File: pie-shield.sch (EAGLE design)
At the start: 15 parts, among them IC6 78L05, IC8 MAX487, X6 RJ45-8L-B

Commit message: before wiring to raspberry
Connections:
- net N$35 renamed SELECT
- net +5V: now also U$2.5V@2, U$2.5V@4, U$2.5V@P5_1
- net GND: now also U$2.GND@14, U$2.GND@20, U$2.GND@6, U$2.GND@P5_7, U$2.GND@P5_8
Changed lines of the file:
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@@
 <pinref part="R22" gate="G$1" pin="1"/>
 <pinref part="R19" gate="G$1" pin="1"/>
+<label x="-33.02" y="78.74" size="1.778" layer="95"/>
+</segment>
+<segment>
+<pinref part="U$2" gate="G$1" pin="5V@2"/>
+<pinref part="U$2" gate="G$1" pin="5V@4"/>
+<wire x1="-73.66" y1="73.66" x2="-86.36" y2="73.66" width="0.1524" layer="91"/>
+<wire x1="-86.36" y1="73.66" x2="-86.36" y2="71.12" width="0.1524" layer="91"/>
+<wire x1="-86.36" y1="71.12" x2="-73.66" y2="71.12" width="0.1524" layer="91"/>
+<label x="-73.66" y="71.12" size="1.778" layer="95"/>
+<label x="-73.66" y="73.66" size="1.778" layer="95"/>
+</segment>
+<segment>
+<pinref part="U$2" gate="G$1" pin="5V@P5_1"/>
+<wire x1="-142.24" y1="38.1" x2="-149.86" y2="38.1" width="0.1524" layer="91"/>
+<label x="-154.94" y="38.1" size="1.778" layer="95"/>
 </segment>
 </net>
-<net name="N$35" class="0">
+<net name="SELECT" class="0">
 <segment>
 <wire x1="-17.78" y1="17.78" x2="-17.78" y2="66.04" width="0.1524" layer="91"/>
 <wire x1="-17.78" y1="66.04" x2="5.08" y2="66.04" width="0.1524" layer="91"/>
 <pinref part="OK3" gate="A" pin="C"/>
+<label x="-27.94" y="17.78" size="1.778" layer="95"/>
 </segment>
 </net>
@@
 <wire x1="-2.54" y1="27.94" x2="-2.54" y2="10.16" width="0.1524" layer="91"/>
 </segment>
+<segment>
+<pinref part="U$2" gate="G$1" pin="GND@14"/>
+<wire x1="-86.36" y1="58.42" x2="-73.66" y2="58.42" width="0.1524" layer="91"/>
+<label x="-73.66" y="58.42" size="1.778" layer="95"/>
+</segment>
+<segment>
+<pinref part="U$2" gate="G$1" pin="GND@20"/>
+<wire x1="-86.36" y1="50.8" x2="-73.66" y2="50.8" width="0.1524" layer="91"/>
+<label x="-73.66" y="50.8" size="1.778" layer="95"/>
+</segment>
+<segment>
+<pinref part="U$2" gate="G$1" pin="GND@P5_8"/>
+<wire x1="-86.36" y1="30.48" x2="-73.66" y2="30.48" width="0.1524" layer="91"/>
+<label x="-73.66" y="30.48" size="1.778" layer="95"/>
+</segment>
+<segment>
+<wire x1="-139.7" y1="63.5" x2="-149.86" y2="63.5" width="0.1524" layer="91"/>
+<label x="-154.94" y="63.5" size="1.778" layer="95"/>
+</segment>
+<segment>
+<pinref part="U$2" gate="G$1" pin="GND@P5_7"/>
+<wire x1="-142.24" y1="30.48" x2="-149.86" y2="30.48" width="0.1524" layer="91"/>
+<label x="-154.94" y="30.48" size="1.778" layer="95"/>
+</segment>
+<segment>
+<pinref part="U$2" gate="G$1" pin="GND@6"/>
+<wire x1="-86.36" y1="68.58" x2="-73.66" y2="68.58" width="0.1524" layer="91"/>
+<label x="-73.66" y="68.58" size="1.778" layer="95"/>
+</segment>
 </net>

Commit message: wired
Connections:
- net RXD_AL: now also U$2.GPIO30
- net SELECT: now also U$2.GPIO31
- net TXD_AL: now also U$2.GPIO29
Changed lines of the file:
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@@
 <pinref part="OK2" gate="A" pin="VO"/>
+</segment>
+<segment>
+<pinref part="U$2" gate="G$1" pin="GPIO30"/>
+<wire x1="-142.24" y1="33.02" x2="-149.86" y2="33.02" width="0.1524" layer="91"/>
+<label x="-157.48" y="33.02" size="1.778" layer="95"/>
 </segment>
 </net>
@@
 <label x="-50.8" y="50.8" size="1.778" layer="95"/>
 <pinref part="OK1" gate="A" pin="C"/>
+</segment>
+<segment>
+<pinref part="U$2" gate="G$1" pin="GPIO29"/>
+<wire x1="-86.36" y1="35.56" x2="-73.66" y2="35.56" width="0.1524" layer="91"/>
+<label x="-73.66" y="35.56" size="1.778" layer="95"/>
 </segment>
 </net>
@@
 <wire x1="-5.08" y1="73.66" x2="-5.08" y2="78.74" width="0.1524" layer="91"/>
 <wire x1="-5.08" y1="78.74" x2="-33.02" y2="78.74" width="0.1524" layer="91"/>
-<wire x1="-40.64" y1="48.26" x2="-40.64" y2="55.88" width="0.1524" layer="91"/>
-<wire x1="-40.64" y1="55.88" x2="-35.56" y2="55.88" width="0.1524" layer="91"/>
-<wire x1="-35.56" y1="48.26" x2="-35.56" y2="55.88" width="0.1524" layer="91"/>
 <wire x1="-7.62" y1="50.8" x2="-7.62" y2="55.88" width="0.1524" layer="91"/>
 <wire x1="-7.62" y1="55.88" x2="-10.16" y2="55.88" width="0.1524" layer="91"/>
 <wire x1="-10.16" y1="55.88" x2="-33.02" y2="55.88" width="0.1524" layer="91"/>
-<wire x1="-33.02" y1="55.88" x2="-35.56" y2="55.88" width="0.1524" layer="91"/>
 <wire x1="-33.02" y1="78.74" x2="-33.02" y2="55.88" width="0.1524" layer="91"/>
 <wire x1="2.54" y1="20.32" x2="-10.16" y2="20.32" width="0.1524" layer="91"/>
 <wire x1="-10.16" y1="20.32" x2="-10.16" y2="55.88" width="0.1524" layer="91"/>
 <junction x="2.54" y="20.32"/>
-<junction x="-35.56" y="55.88"/>
-<junction x="-33.02" y="55.88"/>
 <junction x="-10.16" y="55.88"/>
 <pinref part="OK2" gate="A" pin="VCC"/>
@@
 <label x="-27.94" y="17.78" size="1.778" layer="95"/>
 </segment>
+<segment>
+<pinref part="U$2" gate="G$1" pin="GPIO31"/>
+<wire x1="-86.36" y1="33.02" x2="-73.66" y2="33.02" width="0.1524" layer="91"/>
+<label x="-73.66" y="33.02" size="1.778" layer="95"/>
+</segment>
 </net>

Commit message: rewired to use uart txd, rxd and rts
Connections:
- net RXD_AL: now also U$2.GPIO15,UART0_RXD; no longer U$2.GPIO30
- net SELECT: now also U$2.GPIO17; no longer U$2.GPIO31
- net TXD_AL: now also U$2.GPIO14,UART0_TXD; no longer U$2.GPIO29
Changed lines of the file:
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@@
 </segment>
 <segment>
-<pinref part="U$2" gate="G$1" pin="GPIO30"/>
-<wire x1="-142.24" y1="33.02" x2="-149.86" y2="33.02" width="0.1524" layer="91"/>
-<label x="-157.48" y="33.02" size="1.778" layer="95"/>
+<pinref part="U$2" gate="G$1" pin="GPIO15,UART0_RXD"/>
+<wire x1="-86.36" y1="63.5" x2="-73.66" y2="63.5" width="0.1524" layer="91"/>
+<label x="-73.66" y="63.5" size="1.778" layer="95"/>
 </segment>
 </net>
@@
 </segment>
 <segment>
-<pinref part="U$2" gate="G$1" pin="GPIO29"/>
-<wire x1="-86.36" y1="35.56" x2="-73.66" y2="35.56" width="0.1524" layer="91"/>
-<label x="-73.66" y="35.56" size="1.778" layer="95"/>
+<pinref part="U$2" gate="G$1" pin="GPIO14,UART0_TXD"/>
+<wire x1="-86.36" y1="66.04" x2="-73.66" y2="66.04" width="0.1524" layer="91"/>
+<label x="-73.66" y="66.04" size="1.778" layer="95"/>
 </segment>
 </net>
@@
 </segment>
 <segment>
-<pinref part="U$2" gate="G$1" pin="GPIO31"/>
-<wire x1="-86.36" y1="33.02" x2="-73.66" y2="33.02" width="0.1524" layer="91"/>
-<label x="-73.66" y="33.02" size="1.778" layer="95"/>
+<pinref part="U$2" gate="G$1" pin="GPIO17"/>
+<wire x1="-142.24" y1="60.96" x2="-149.86" y2="60.96" width="0.1524" layer="91"/>
+<label x="-160.02" y="60.96" size="1.778" layer="95"/>
 </segment>
 </net>

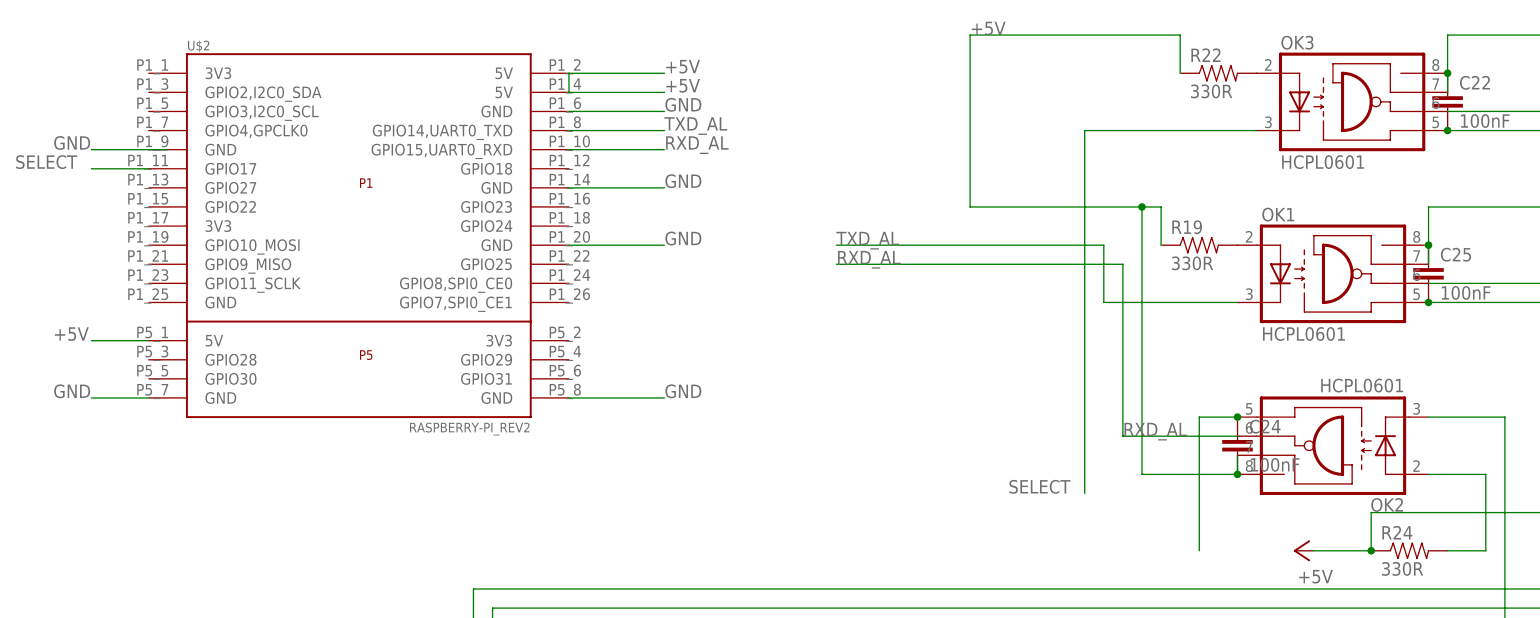
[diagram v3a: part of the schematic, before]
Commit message: set optocouplers on pie side to 3.3V levels
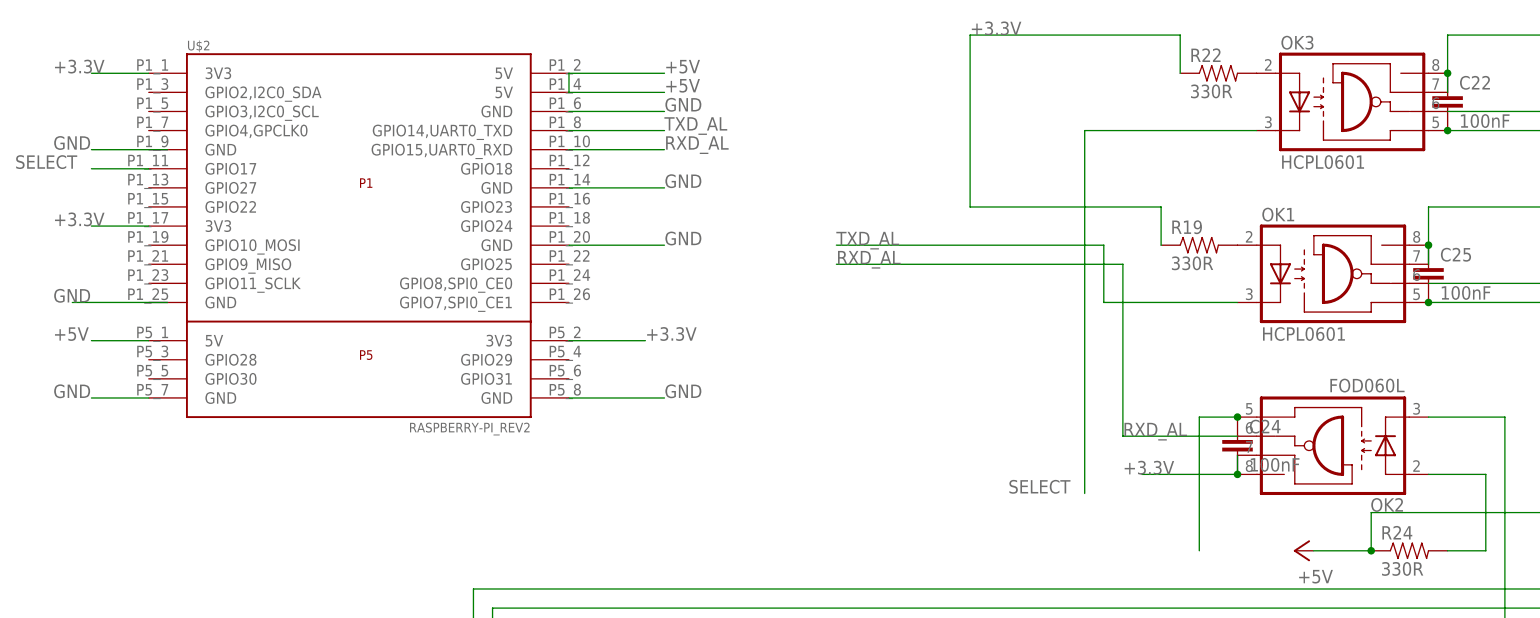
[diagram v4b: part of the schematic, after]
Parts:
- OK2: value HCPL0601 -> FOD060L
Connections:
- new net +3.3V: C24.2, OK2.VCC, OK2.VE, R19.1, R22.1, U$2.3V3@1, U$2.3V3@17, U$2.3V3@P5_2
- net +5V: no longer C24.2, OK2.VCC, OK2.VE, R19.1, R22.1
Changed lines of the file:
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@@
 <part name="P+12" library="supply1" deviceset="+12V" device=""/>
 <part name="OK1" library="optocoupler" deviceset="HCPL0601" device=""/>
-<part name="OK2" library="optocoupler" deviceset="HCPL0601" device=""/>
+<part name="OK2" library="optocoupler" deviceset="HCPL0601" device="" value="FOD060L"/>
 <part name="C24" library="SparkFun" deviceset="CAP" device="0805" value="100nF"/>
 <part name="C25" library="SparkFun" deviceset="CAP" device="0805" value="100nF"/>
@@
 <net name="+5V" class="0">
 <segment>
-<wire x1="2.54" y1="22.86" x2="2.54" y2="20.32" width="0.1524" layer="91"/>
-<wire x1="-5.08" y1="73.66" x2="-5.08" y2="78.74" width="0.1524" layer="91"/>
-<wire x1="-5.08" y1="78.74" x2="-33.02" y2="78.74" width="0.1524" layer="91"/>
-<wire x1="-7.62" y1="50.8" x2="-7.62" y2="55.88" width="0.1524" layer="91"/>
-<wire x1="-7.62" y1="55.88" x2="-10.16" y2="55.88" width="0.1524" layer="91"/>
-<wire x1="-10.16" y1="55.88" x2="-33.02" y2="55.88" width="0.1524" layer="91"/>
-<wire x1="-33.02" y1="78.74" x2="-33.02" y2="55.88" width="0.1524" layer="91"/>
-<wire x1="2.54" y1="20.32" x2="-10.16" y2="20.32" width="0.1524" layer="91"/>
-<wire x1="-10.16" y1="20.32" x2="-10.16" y2="55.88" width="0.1524" layer="91"/>
-<junction x="2.54" y="20.32"/>
-<junction x="-10.16" y="55.88"/>
-<pinref part="OK2" gate="A" pin="VCC"/>
-<pinref part="C24" gate="G$1" pin="2"/>
-<pinref part="OK2" gate="A" pin="VE"/>
-<pinref part="R22" gate="G$1" pin="1"/>
-<pinref part="R19" gate="G$1" pin="1"/>
-<label x="-33.02" y="78.74" size="1.778" layer="95"/>
-</segment>
-<segment>
 <pinref part="U$2" gate="G$1" pin="5V@2"/>
 <pinref part="U$2" gate="G$1" pin="5V@4"/>
@@
 <label x="-73.66" y="68.58" size="1.778" layer="95"/>
 </segment>
-</net>
+<segment>
+<wire x1="-139.7" y1="43.18" x2="-152.4" y2="43.18" width="0.1524" layer="91"/>
+<label x="-154.94" y="43.18" size="1.778" layer="95"/>
+</segment>
+</net>
+<net name="+3.3V" class="0">
+<segment>
+<pinref part="OK2" gate="A" pin="VE"/>
+<wire x1="2.54" y1="22.86" x2="2.54" y2="20.32" width="0.1524" layer="91"/>
+<junction x="2.54" y="20.32"/>
+<pinref part="OK2" gate="A" pin="VCC"/>
+<pinref part="C24" gate="G$1" pin="2"/>
+<wire x1="2.54" y1="20.32" x2="-10.16" y2="20.32" width="0.1524" layer="91"/>
+<label x="-12.7" y="20.32" size="1.778" layer="95"/>
+</segment>
+<segment>
+<pinref part="U$2" gate="G$1" pin="3V3@1"/>
+<wire x1="-142.24" y1="73.66" x2="-149.86" y2="73.66" width="0.1524" layer="91"/>
+<label x="-154.94" y="73.66" size="1.778" layer="95"/>
+</segment>
+<segment>
+<pinref part="U$2" gate="G$1" pin="3V3@17"/>
+<wire x1="-142.24" y1="53.34" x2="-149.86" y2="53.34" width="0.1524" layer="91"/>
+<label x="-154.94" y="53.34" size="1.778" layer="95"/>
+</segment>
+<segment>
+<pinref part="U$2" gate="G$1" pin="3V3@P5_2"/>
+<wire x1="-86.36" y1="38.1" x2="-76.2" y2="38.1" width="0.1524" layer="91"/>
+<label x="-76.2" y="38.1" size="1.778" layer="95"/>
+</segment>
+<segment>
+<wire x1="-5.08" y1="73.66" x2="-5.08" y2="78.74" width="0.1524" layer="91"/>
+<wire x1="-5.08" y1="78.74" x2="-33.02" y2="78.74" width="0.1524" layer="91"/>
+<wire x1="-7.62" y1="50.8" x2="-7.62" y2="55.88" width="0.1524" layer="91"/>
+<wire x1="-7.62" y1="55.88" x2="-33.02" y2="55.88" width="0.1524" layer="91"/>
+<wire x1="-33.02" y1="78.74" x2="-33.02" y2="55.88" width="0.1524" layer="91"/>
+<pinref part="R22" gate="G$1" pin="1"/>
+<pinref part="R19" gate="G$1" pin="1"/>
+<label x="-33.02" y="78.74" size="1.778" layer="95"/>
+</segment>
+</net>
